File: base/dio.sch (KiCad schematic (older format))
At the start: 28 parts

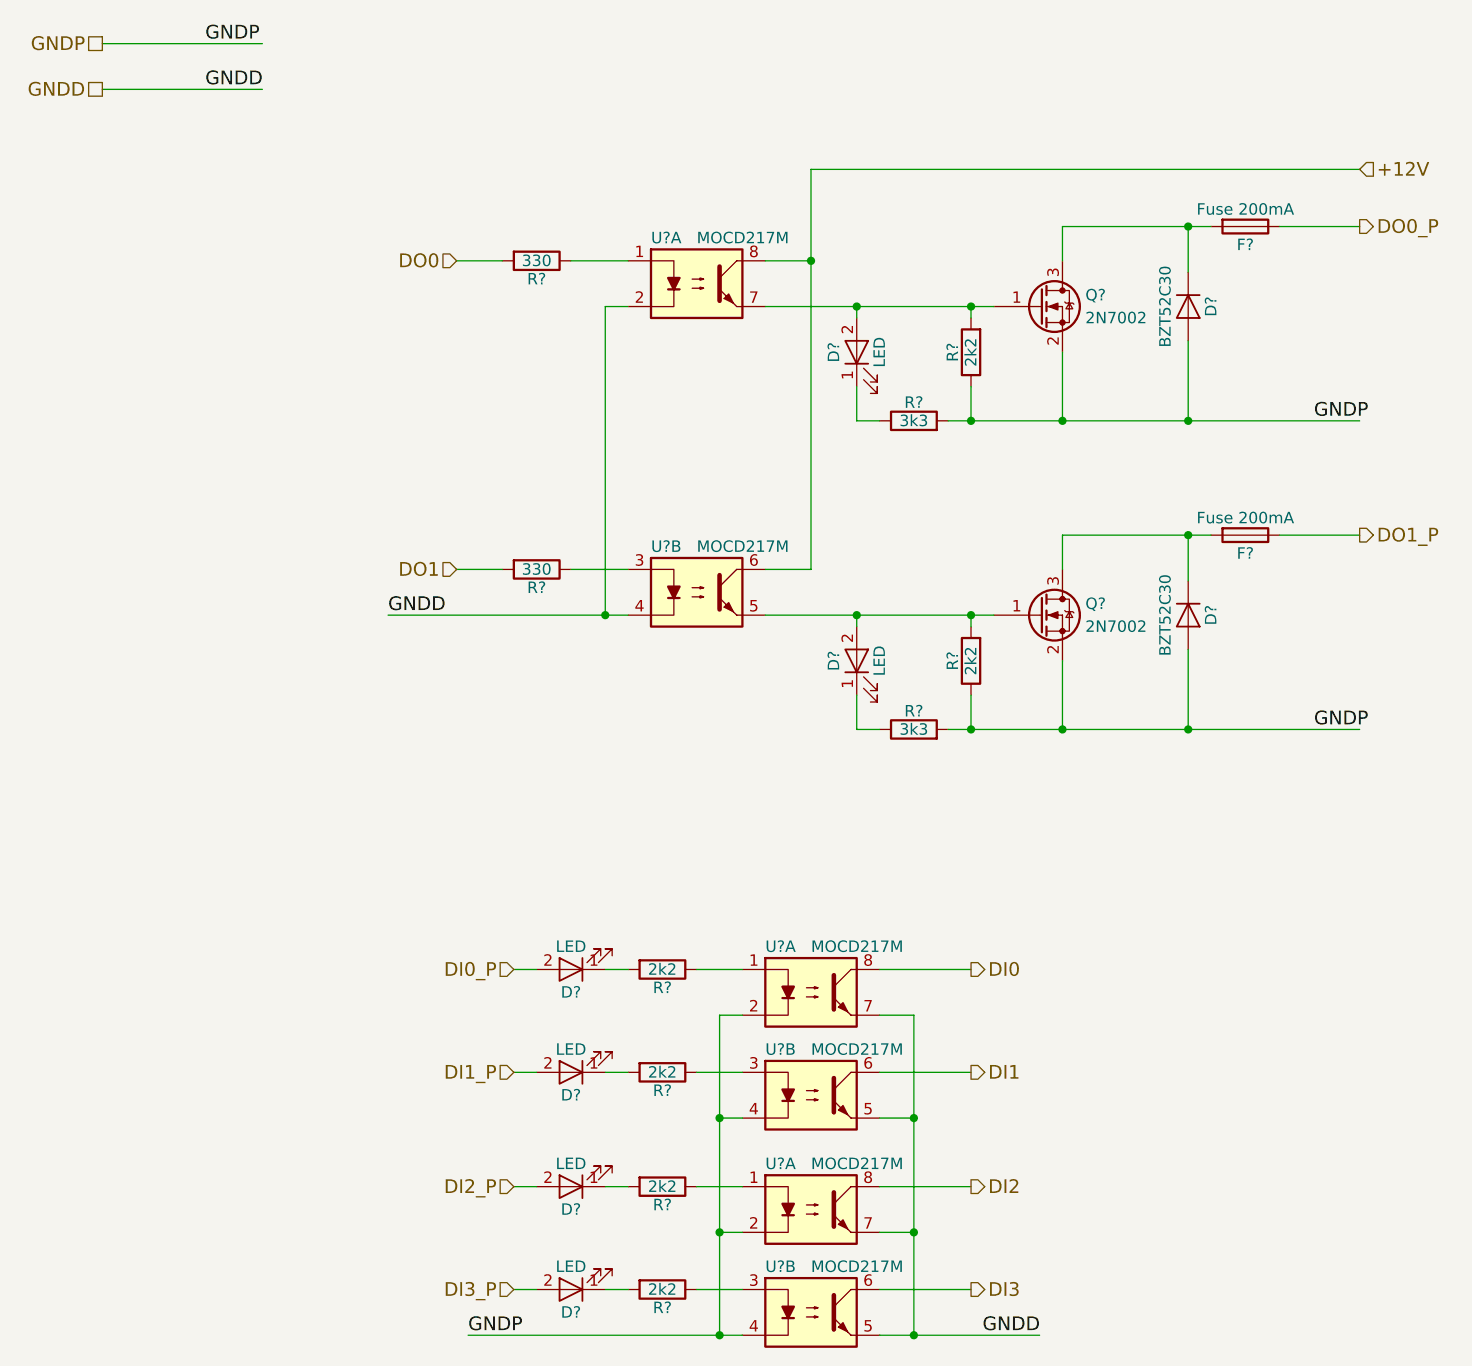
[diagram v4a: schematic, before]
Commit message: Update base board: 1. Add extra analog voltage input to core board.   -> update pinmux 2. Assign most footprints. 3. Generate netlist. 4. Add core_sf board. 5. Add kicad_symbols library submodule.
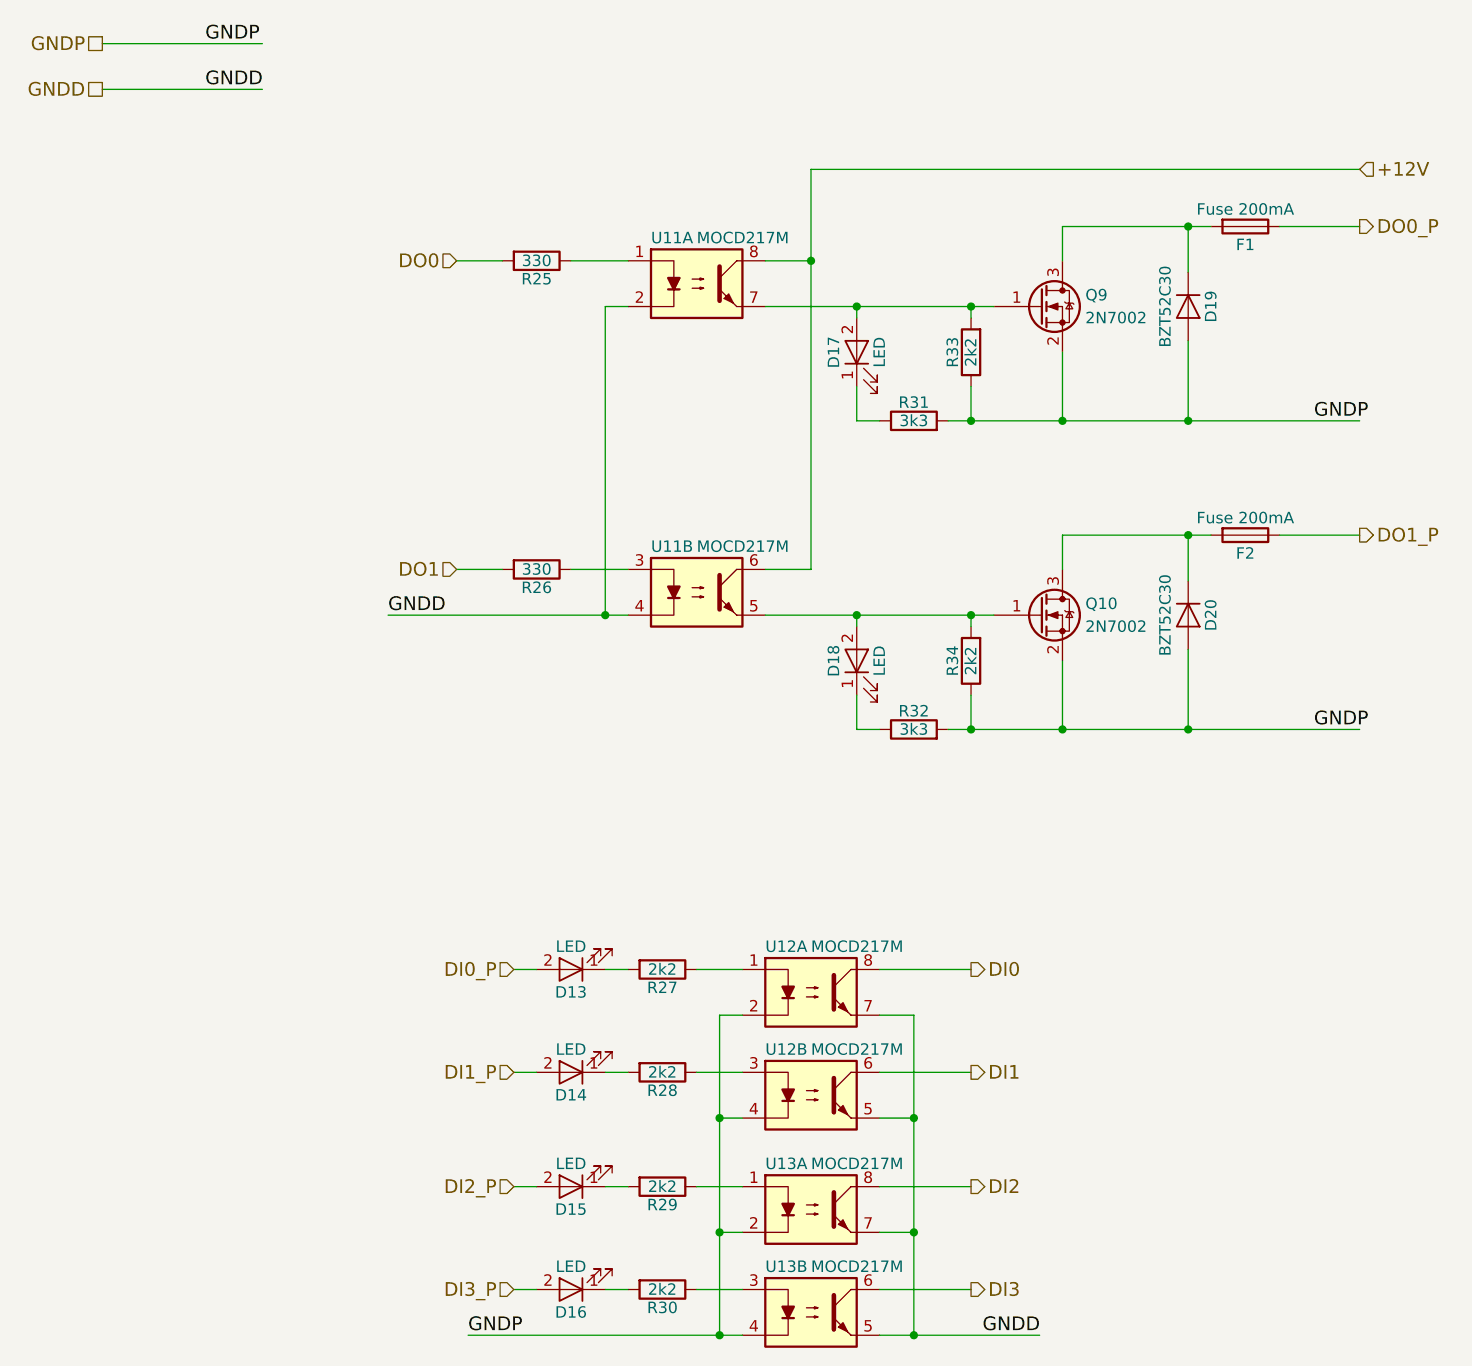
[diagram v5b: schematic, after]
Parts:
- D13, D14, D15, D16, D17, D18: renamed from D?; footprint (none) -> LED_SMD:LED_0603_1608Metric
- D19, D20: renamed from D?; footprint (none) -> Diode_SMD:D_SOD-123
- F1, F2: renamed from F?; footprint (none) -> Fuse:Fuse_1206_3216Metric
- Q10, Q9: renamed from Q?; footprint (none) -> Package_TO_SOT_SMD:SOT-23
- R25, R26, R27, R28, R29, R30, R31, R32, R33, R34: renamed from R?; footprint (none) -> Resistor_SMD:R_0603_1608Metric
- U11, U12, U13: renamed from U?; footprint Housings_SOIC:SOIC-8_3.9x4.9mm_Pitch1.27mm -> Package_SOIC:SOIC-8_3.9x4.9mm_P1.27mm
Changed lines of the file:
@@
 GNDP
 $Comp
-L MOCD217M U?
+L MOCD217M U12
 U 1 1 5A43CCC9
 P 4150 5000
-F 0 "U?" H 3950 5200 50  0000 L CNN
+F 0 "U12" H 3950 5200 50  0000 L CNN
 F 1 "MOCD217M" H 4150 5200 50  0000 L CNN
-F 2 "Housings_SOIC:SOIC-8_3.9x4.9mm_Pitch1.27mm" H 3950 4800 50  0001 L CIN
+F 2 "Package_SOIC:SOIC-8_3.9x4.9mm_P1.27mm" H 3950 4800 50  0001 L CIN
 F 3 "" H 4150 5000 50  0001 L CNN
 	1    4150 5000
@@
 $EndComp
 $Comp
-L MOCD217M U?
+L MOCD217M U12
 U 2 1 5A43CCE0
 P 4150 5450
-F 0 "U?" H 3950 5650 50  0000 L CNN
+F 0 "U12" H 3950 5650 50  0000 L CNN
 F 1 "MOCD217M" H 4150 5650 50  0000 L CNN
-F 2 "Housings_SOIC:SOIC-8_3.9x4.9mm_Pitch1.27mm" H 3950 5250 50  0001 L CIN
+F 2 "Package_SOIC:SOIC-8_3.9x4.9mm_P1.27mm" H 3950 5250 50  0001 L CIN
 F 3 "" H 4150 5450 50  0001 L CNN
 	2    4150 5450
@@
 $EndComp
 $Comp
-L LED D?
+L LED D13
 U 1 1 5A43CD4D
 P 3100 4900
-F 0 "D?" H 3100 5000 50  0000 C CNN
+F 0 "D13" H 3100 5000 50  0000 C CNN
 F 1 "LED" H 3100 4800 50  0000 C CNN
-F 2 "" H 3100 4900 50  0001 C CNN
+F 2 "LED_SMD:LED_0603_1608Metric" H 3100 4900 50  0001 C CNN
 F 3 "" H 3100 4900 50  0001 C CNN
 	1    3100 4900
@@
 $EndComp
 $Comp
-L R R?
+L R R27
 U 1 1 5A43CDFC
 P 3500 4900
-F 0 "R?" V 3580 4900 50  0000 C CNN
+F 0 "R27" V 3580 4900 50  0000 C CNN
 F 1 "2k2" V 3500 4900 50  0000 C CNN
-F 2 "" V 3430 4900 50  0001 C CNN
+F 2 "Resistor_SMD:R_0603_1608Metric" V 3430 4900 50  0001 C CNN
 F 3 "" H 3500 4900 50  0001 C CNN
 	1    3500 4900
@@
 $EndComp
 $Comp
-L LED D?
+L LED D14
 U 1 1 5A43CE85
 P 3100 5350
-F 0 "D?" H 3100 5450 50  0000 C CNN
+F 0 "D14" H 3100 5450 50  0000 C CNN
 F 1 "LED" H 3100 5250 50  0000 C CNN
-F 2 "" H 3100 5350 50  0001 C CNN
+F 2 "LED_SMD:LED_0603_1608Metric" H 3100 5350 50  0001 C CNN
 F 3 "" H 3100 5350 50  0001 C CNN
 	1    3100 5350
@@
 $EndComp
 $Comp
-L R R?
+L R R28
 U 1 1 5A43CEB2
 P 3500 5350
-F 0 "R?" V 3580 5350 50  0000 C CNN
+F 0 "R28" V 3580 5350 50  0000 C CNN
 F 1 "2k2" V 3500 5350 50  0000 C CNN
-F 2 "" V 3430 5350 50  0001 C CNN
+F 2 "Resistor_SMD:R_0603_1608Metric" V 3430 5350 50  0001 C CNN
 F 3 "" H 3500 5350 50  0001 C CNN
 	1    3500 5350
@@
 $EndComp
 $Comp
-L MOCD217M U?
+L MOCD217M U13
 U 1 1 5A43D0F4
 P 4150 5950
-F 0 "U?" H 3950 6150 50  0000 L CNN
+F 0 "U13" H 3950 6150 50  0000 L CNN
 F 1 "MOCD217M" H 4150 6150 50  0000 L CNN
-F 2 "Housings_SOIC:SOIC-8_3.9x4.9mm_Pitch1.27mm" H 3950 5750 50  0001 L CIN
+F 2 "Package_SOIC:SOIC-8_3.9x4.9mm_P1.27mm" H 3950 5750 50  0001 L CIN
 F 3 "" H 4150 5950 50  0001 L CNN
 	1    4150 5950
@@
 $EndComp
 $Comp
-L MOCD217M U?
+L MOCD217M U13
 U 2 1 5A43D129
 P 4150 6400
-F 0 "U?" H 3950 6600 50  0000 L CNN
+F 0 "U13" H 3950 6600 50  0000 L CNN
 F 1 "MOCD217M" H 4150 6600 50  0000 L CNN
-F 2 "Housings_SOIC:SOIC-8_3.9x4.9mm_Pitch1.27mm" H 3950 6200 50  0001 L CIN
+F 2 "Package_SOIC:SOIC-8_3.9x4.9mm_P1.27mm" H 3950 6200 50  0001 L CIN
 F 3 "" H 4150 6400 50  0001 L CNN
 	2    4150 6400
@@
 $EndComp
 $Comp
-L LED D?
+L LED D15
 U 1 1 5A43D248
 P 3100 5850
-F 0 "D?" H 3100 5950 50  0000 C CNN
+F 0 "D15" H 3100 5950 50  0000 C CNN
 F 1 "LED" H 3100 5750 50  0000 C CNN
-F 2 "" H 3100 5850 50  0001 C CNN
+F 2 "LED_SMD:LED_0603_1608Metric" H 3100 5850 50  0001 C CNN
 F 3 "" H 3100 5850 50  0001 C CNN
 	1    3100 5850
@@
 $EndComp
 $Comp
-L R R?
+L R R29
 U 1 1 5A43D285
 P 3500 5850
-F 0 "R?" V 3580 5850 50  0000 C CNN
+F 0 "R29" V 3580 5850 50  0000 C CNN
 F 1 "2k2" V 3500 5850 50  0000 C CNN
-F 2 "" V 3430 5850 50  0001 C CNN
+F 2 "Resistor_SMD:R_0603_1608Metric" V 3430 5850 50  0001 C CNN
 F 3 "" H 3500 5850 50  0001 C CNN
 	1    3500 5850
@@
 $EndComp
 $Comp
-L LED D?
+L LED D16
 U 1 1 5A43D2D5
 P 3100 6300
-F 0 "D?" H 3100 6400 50  0000 C CNN
+F 0 "D16" H 3100 6400 50  0000 C CNN
 F 1 "LED" H 3100 6200 50  0000 C CNN
-F 2 "" H 3100 6300 50  0001 C CNN
+F 2 "LED_SMD:LED_0603_1608Metric" H 3100 6300 50  0001 C CNN
 F 3 "" H 3100 6300 50  0001 C CNN
 	1    3100 6300
@@
 $EndComp
 $Comp
-L R R?
+L R R30
 U 1 1 5A43D320
 P 3500 6300
-F 0 "R?" V 3580 6300 50  0000 C CNN
+F 0 "R30" V 3580 6300 50  0000 C CNN
 F 1 "2k2" V 3500 6300 50  0000 C CNN
-F 2 "" V 3430 6300 50  0001 C CNN
+F 2 "Resistor_SMD:R_0603_1608Metric" V 3430 6300 50  0001 C CNN
 F 3 "" H 3500 6300 50  0001 C CNN
 	1    3500 6300
@@
 $EndComp
 $Comp
-L MOCD217M U?
+L MOCD217M U11
 U 1 1 5A43D9A7
 P 3650 1900
-F 0 "U?" H 3450 2100 50  0000 L CNN
+F 0 "U11" H 3450 2100 50  0000 L CNN
 F 1 "MOCD217M" H 3650 2100 50  0000 L CNN
-F 2 "Housings_SOIC:SOIC-8_3.9x4.9mm_Pitch1.27mm" H 3450 1700 50  0001 L CIN
+F 2 "Package_SOIC:SOIC-8_3.9x4.9mm_P1.27mm" H 3450 1700 50  0001 L CIN
 F 3 "" H 3650 1900 50  0001 L CNN
 	1    3650 1900
@@
 $EndComp
 $Comp
-L MOCD217M U?
+L MOCD217M U11
 U 2 1 5A43DABA
 P 3650 3250
-F 0 "U?" H 3450 3450 50  0000 L CNN
+F 0 "U11" H 3450 3450 50  0000 L CNN
 F 1 "MOCD217M" H 3650 3450 50  0000 L CNN
-F 2 "Housings_SOIC:SOIC-8_3.9x4.9mm_Pitch1.27mm" H 3450 3050 50  0001 L CIN
+F 2 "Package_SOIC:SOIC-8_3.9x4.9mm_P1.27mm" H 3450 3050 50  0001 L CIN
 F 3 "" H 3650 3250 50  0001 L CNN
 	2    3650 3250
@@
 $EndComp
 $Comp
-L Q_NMOS_GSD Q?
+L Q_NMOS_GSD Q9
 U 1 1 5A43DD59
 P 5150 2000
-F 0 "Q?" H 5350 2050 50  0000 L CNN
+F 0 "Q9" H 5350 2050 50  0000 L CNN
 F 1 "2N7002" H 5350 1950 50  0000 L CNN
-F 2 "" H 5350 2100 50  0001 C CNN
+F 2 "Package_TO_SOT_SMD:SOT-23" H 5350 2100 50  0001 C CNN
 F 3 "" H 5150 2000 50  0001 C CNN
 	1    5150 2000
@@
 $EndComp
 $Comp
-L Fuse F?
+L Fuse F1
 U 1 1 5A43DEA4
 P 6050 1650
-F 0 "F?" V 6130 1650 50  0000 C CNN
+F 0 "F1" V 6130 1650 50  0000 C CNN
 F 1 "Fuse 200mA" V 5975 1650 50  0000 C CNN
-F 2 "" V 5980 1650 50  0001 C CNN
+F 2 "Fuse:Fuse_1206_3216Metric" V 5980 1650 50  0001 C CNN
 F 3 "" H 6050 1650 50  0001 C CNN
 	1    6050 1650
@@
 $EndComp
 $Comp
-L D D?
+L D D19
 U 1 1 5A43DF8B
 P 5800 2000
-F 0 "D?" H 5800 2100 50  0000 C CNN
+F 0 "D19" H 5800 2100 50  0000 C CNN
 F 1 "BZT52C30" H 5800 1900 50  0000 C CNN
-F 2 "" H 5800 2000 50  0001 C CNN
+F 2 "Diode_SMD:D_SOD-123" H 5800 2000 50  0001 C CNN
 F 3 "" H 5800 2000 50  0001 C CNN
 	1    5800 2000
@@
 $EndComp
 $Comp
-L R R?
+L R R25
 U 1 1 5A43E17A
 P 2950 1800
-F 0 "R?" V 3030 1800 50  0000 C CNN
+F 0 "R25" V 3030 1800 50  0000 C CNN
 F 1 "330" V 2950 1800 50  0000 C CNN
-F 2 "" V 2880 1800 50  0001 C CNN
+F 2 "Resistor_SMD:R_0603_1608Metric" V 2880 1800 50  0001 C CNN
 F 3 "" H 2950 1800 50  0001 C CNN
 	1    2950 1800
@@
 $EndComp
 $Comp
-L R R?
+L R R26
 U 1 1 5A43E449
 P 2950 3150
-F 0 "R?" V 3030 3150 50  0000 C CNN
+F 0 "R26" V 3030 3150 50  0000 C CNN
 F 1 "330" V 2950 3150 50  0000 C CNN
-F 2 "" V 2880 3150 50  0001 C CNN
+F 2 "Resistor_SMD:R_0603_1608Metric" V 2880 3150 50  0001 C CNN
 F 3 "" H 2950 3150 50  0001 C CNN
 	1    2950 3150
@@
 GNDP
 $Comp
-L R R?
+L R R33
 U 1 1 5A43F47F
 P 4850 2200
-F 0 "R?" V 4930 2200 50  0000 C CNN
+F 0 "R33" V 4930 2200 50  0000 C CNN
 F 1 "2k2" V 4850 2200 50  0000 C CNN
-F 2 "" V 4780 2200 50  0001 C CNN
+F 2 "Resistor_SMD:R_0603_1608Metric" V 4780 2200 50  0001 C CNN
 F 3 "" H 4850 2200 50  0001 C CNN
 	1    4850 2200
@@
 $EndComp
 $Comp
-L LED D?
+L LED D17
 U 1 1 5A43F540
 P 4350 2200
-F 0 "D?" H 4350 2300 50  0000 C CNN
+F 0 "D17" H 4350 2300 50  0000 C CNN
 F 1 "LED" H 4350 2100 50  0000 C CNN
-F 2 "" H 4350 2200 50  0001 C CNN
+F 2 "LED_SMD:LED_0603_1608Metric" H 4350 2200 50  0001 C CNN
 F 3 "" H 4350 2200 50  0001 C CNN
 	1    4350 2200
@@
 $EndComp
 $Comp
-L R R?
+L R R31
 U 1 1 5A43F82A
 P 4600 2500
-F 0 "R?" V 4680 2500 50  0000 C CNN
+F 0 "R31" V 4680 2500 50  0000 C CNN
 F 1 "3k3" V 4600 2500 50  0000 C CNN
-F 2 "" V 4530 2500 50  0001 C CNN
+F 2 "Resistor_SMD:R_0603_1608Metric" V 4530 2500 50  0001 C CNN
 F 3 "" H 4600 2500 50  0001 C CNN
 	1    4600 2500
@@
 GNDP
 $Comp
-L Q_NMOS_GSD Q?
+L Q_NMOS_GSD Q10
 U 1 1 5A440176
 P 5150 3350
-F 0 "Q?" H 5350 3400 50  0000 L CNN
+F 0 "Q10" H 5350 3400 50  0000 L CNN
 F 1 "2N7002" H 5350 3300 50  0000 L CNN
-F 2 "" H 5350 3450 50  0001 C CNN
+F 2 "Package_TO_SOT_SMD:SOT-23" H 5350 3450 50  0001 C CNN
 F 3 "" H 5150 3350 50  0001 C CNN
 	1    5150 3350
@@
 $EndComp
 $Comp
-L Fuse F?
+L Fuse F2
 U 1 1 5A44017C
 P 6050 3000
-F 0 "F?" V 6130 3000 50  0000 C CNN
+F 0 "F2" V 6130 3000 50  0000 C CNN
 F 1 "Fuse 200mA" V 5975 3000 50  0000 C CNN
-F 2 "" V 5980 3000 50  0001 C CNN
+F 2 "Fuse:Fuse_1206_3216Metric" V 5980 3000 50  0001 C CNN
 F 3 "" H 6050 3000 50  0001 C CNN
 	1    6050 3000
@@
 $EndComp
 $Comp
-L D D?
+L D D20
 U 1 1 5A440182
 P 5800 3350
-F 0 "D?" H 5800 3450 50  0000 C CNN
+F 0 "D20" H 5800 3450 50  0000 C CNN
 F 1 "BZT52C30" H 5800 3250 50  0000 C CNN
-F 2 "" H 5800 3350 50  0001 C CNN
+F 2 "Diode_SMD:D_SOD-123" H 5800 3350 50  0001 C CNN
 F 3 "" H 5800 3350 50  0001 C CNN
 	1    5800 3350
@@
 $EndComp
 $Comp
-L R R?
+L R R34
 U 1 1 5A440188
 P 4850 3550
-F 0 "R?" V 4930 3550 50  0000 C CNN
+F 0 "R34" V 4930 3550 50  0000 C CNN
 F 1 "2k2" V 4850 3550 50  0000 C CNN
-F 2 "" V 4780 3550 50  0001 C CNN
+F 2 "Resistor_SMD:R_0603_1608Metric" V 4780 3550 50  0001 C CNN
 F 3 "" H 4850 3550 50  0001 C CNN
 	1    4850 3550
@@
 $EndComp
 $Comp
-L LED D?
+L LED D18
 U 1 1 5A44018E
 P 4350 3550
-F 0 "D?" H 4350 3650 50  0000 C CNN
+F 0 "D18" H 4350 3650 50  0000 C CNN
 F 1 "LED" H 4350 3450 50  0000 C CNN
-F 2 "" H 4350 3550 50  0001 C CNN
+F 2 "LED_SMD:LED_0603_1608Metric" H 4350 3550 50  0001 C CNN
 F 3 "" H 4350 3550 50  0001 C CNN
 	1    4350 3550
@@
 $EndComp
 $Comp
-L R R?
+L R R32
 U 1 1 5A440194
 P 4600 3850
-F 0 "R?" V 4680 3850 50  0000 C CNN
+F 0 "R32" V 4680 3850 50  0000 C CNN
 F 1 "3k3" V 4600 3850 50  0000 C CNN
-F 2 "" V 4530 3850 50  0001 C CNN
+F 2 "Resistor_SMD:R_0603_1608Metric" V 4530 3850 50  0001 C CNN
 F 3 "" H 4600 3850 50  0001 C CNN
 	1    4600 3850

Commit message: temp-sens-fan was created
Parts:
- added Q?: 2N7002, Package_TO_SOT_SMD:SOT-23, symbol Q_NMOS_GSD
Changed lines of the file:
@@
 LIBS:texas
 LIBS:opto
+LIBS:maxim
 LIBS:4hbd-base-cache
 EELAYER 25 0
@@
 Text Label 2300 3350 0    60   ~ 0
 GNDD
+$Comp
+L Q_NMOS_GSD Q?
+U 1 1 5A455FDA
+P 3750 1900
+F 0 "Q?" H 3950 1950 50  0000 L CNN
+F 1 "2N7002" H 3950 1850 50  0000 L CNN
+F 2 "Package_TO_SOT_SMD:SOT-23" H 3950 2000 50  0001 C CNN
+F 3 "" H 3750 1900 50  0001 C CNN
+	1    3750 1900
+	1    0    0    -1
+$EndComp
 $EndSCHEMATC

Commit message: annotate sch
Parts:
- gave numbers to parts that had none: 1
- renumbered Q9 to Q10, Q10 to Q11
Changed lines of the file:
@@
 $EndComp
 $Comp
-L Q_NMOS_GSD Q9
+L Q_NMOS_GSD Q10
 U 1 1 5A43DD59
 P 5150 2000
-F 0 "Q9" H 5350 2050 50  0000 L CNN
+F 0 "Q10" H 5350 2050 50  0000 L CNN
 F 1 "2N7002" H 5350 1950 50  0000 L CNN
 F 2 "Package_TO_SOT_SMD:SOT-23" H 5350 2100 50  0001 C CNN
@@
 GNDP
 $Comp
-L Q_NMOS_GSD Q10
+L Q_NMOS_GSD Q11
 U 1 1 5A440176
 P 5150 3350
-F 0 "Q10" H 5350 3400 50  0000 L CNN
+F 0 "Q11" H 5350 3400 50  0000 L CNN
 F 1 "2N7002" H 5350 3300 50  0000 L CNN
 F 2 "Package_TO_SOT_SMD:SOT-23" H 5350 3450 50  0001 C CNN
@@
 GNDD
 $Comp
-L Q_NMOS_GSD Q?
+L Q_NMOS_GSD Q9
 U 1 1 5A455FDA
 P 3750 1900
-F 0 "Q?" H 3950 1950 50  0000 L CNN
+F 0 "Q9" H 3950 1950 50  0000 L CNN
 F 1 "2N7002" H 3950 1850 50  0000 L CNN
 F 2 "Package_TO_SOT_SMD:SOT-23" H 3950 2000 50  0001 C CNN
